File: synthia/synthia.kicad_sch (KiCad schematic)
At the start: 119 parts, among them J1 MJ-63022B, J2 SJ3-35083C-TR, J3 PJ-007, J4 SDS-50J, Q1 IRF9540N, U1 TLV272IP, U2 STM32H750ZBT6, U3 LD1117V33, U4 PVA1EEH31.2NV2, U5 PVA1EEH31.2NV2, U6 ATS08A-E

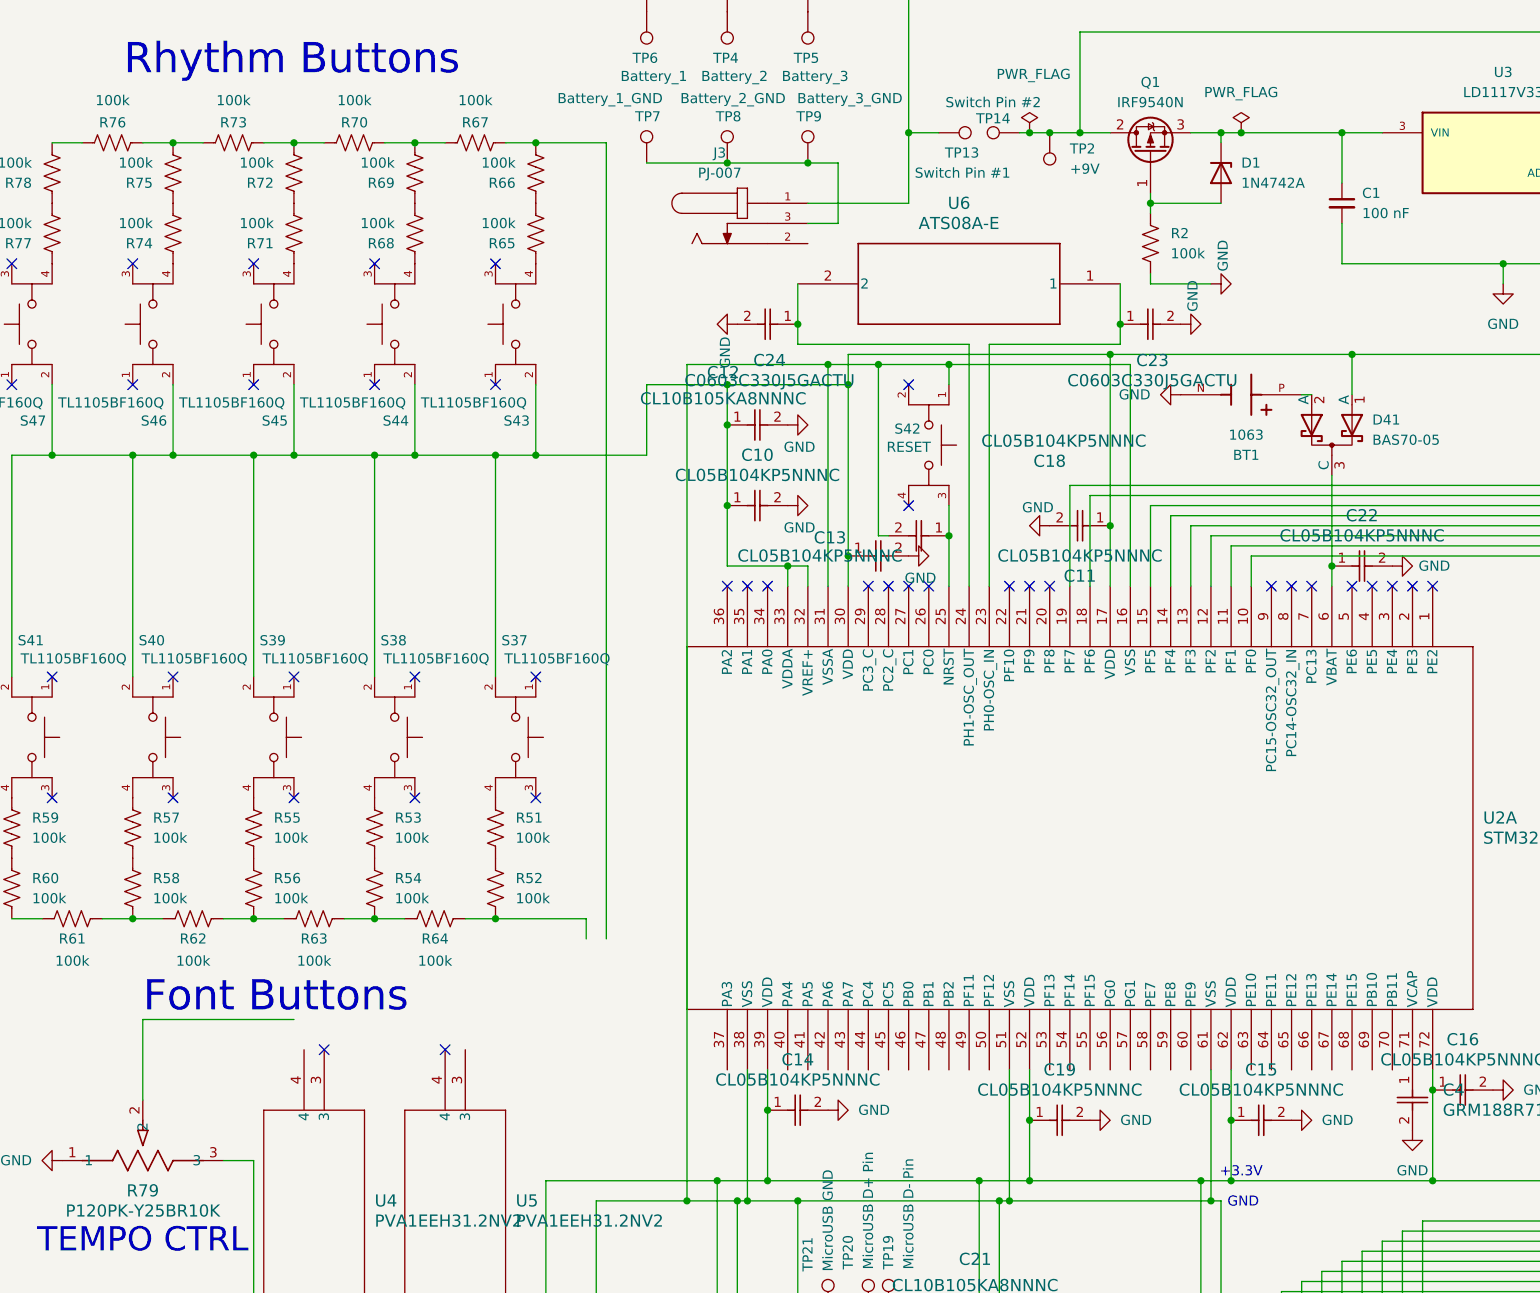
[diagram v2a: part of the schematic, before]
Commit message: made 3D model of current PCB, will likely be updated and replaced when needed
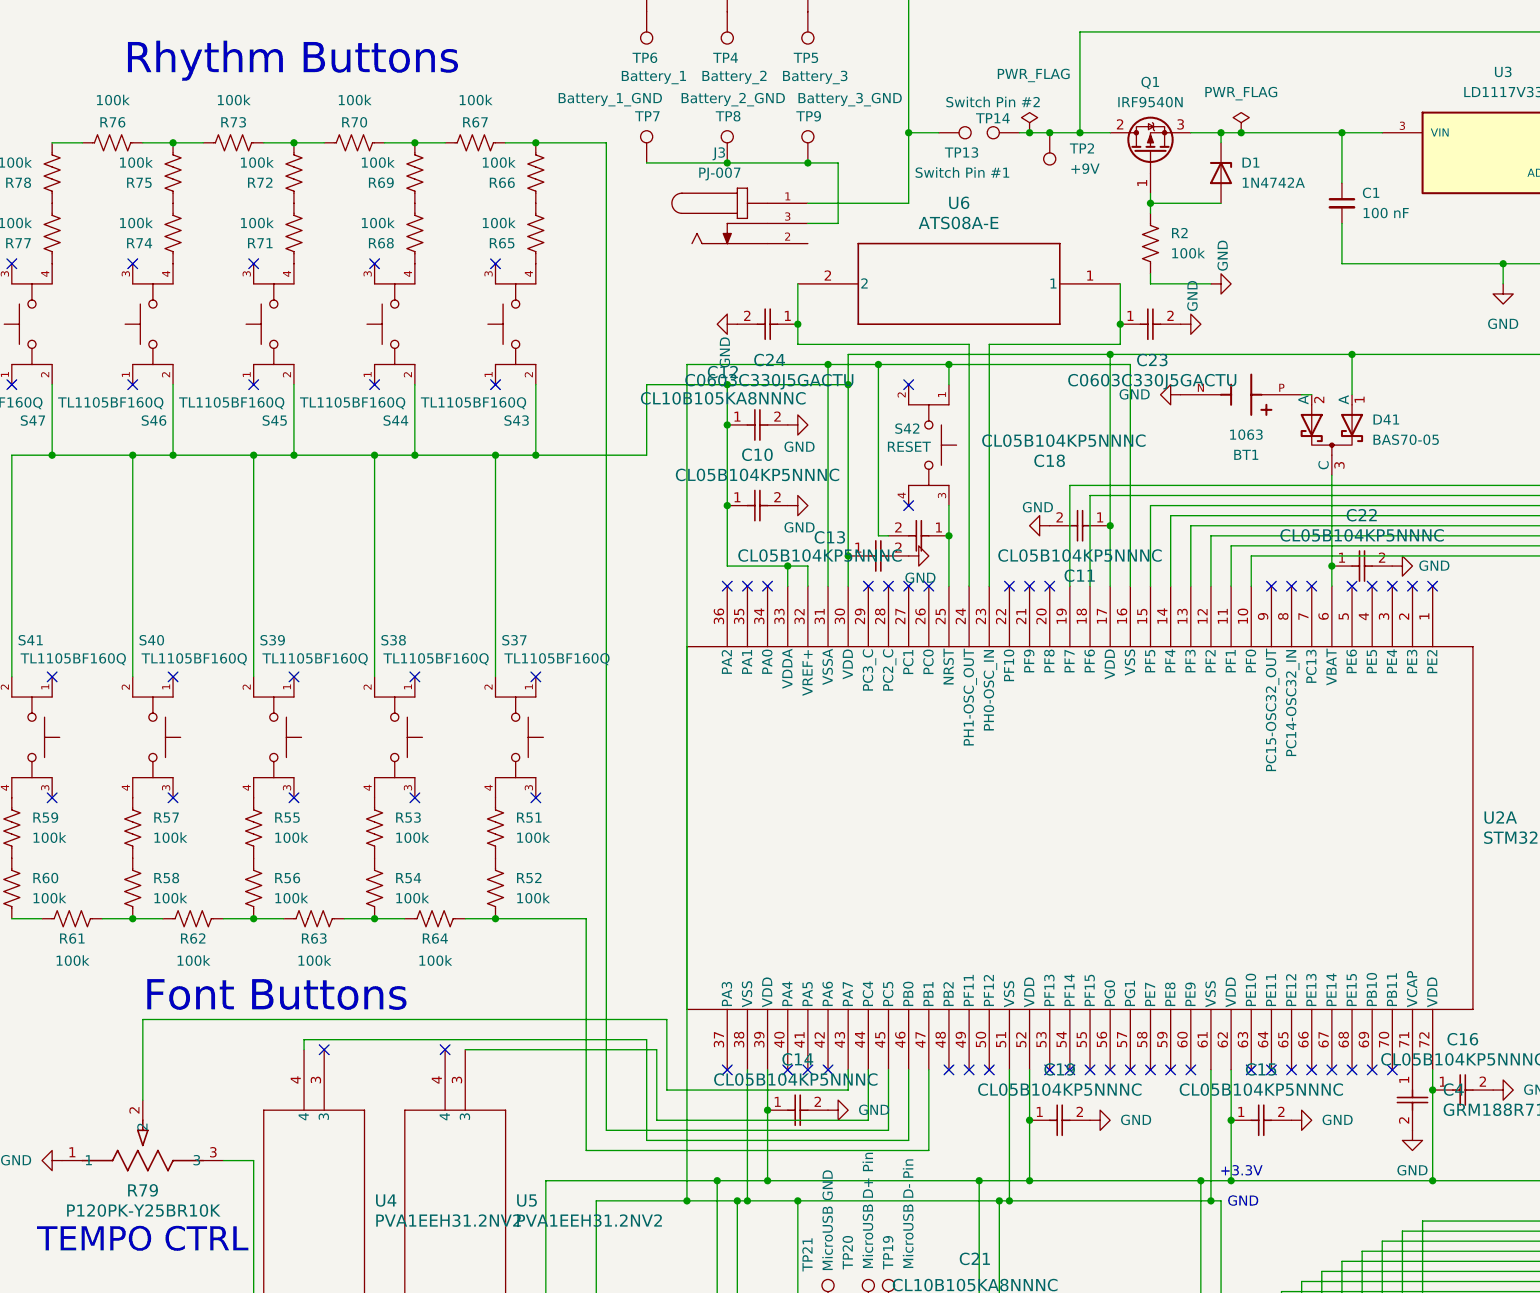
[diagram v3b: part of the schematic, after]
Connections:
- net at R66.2, R67.1: now also U2.45 (PC5)
- net at R52.2, R64.2: now also U2.47 (PB1)
- net at U4.4: now also U2.46 (PB0)
- net at R79.2: now also U2.43 (PA7)
- net at U2.44 (PC4): now also U5.3
- no-connect marks 86 -> 109
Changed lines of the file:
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@@
 	)
 	(no_connect
+		(at 134.62 161.29)
+	)
+	(no_connect
 		(at 120.65 205.74)
 	)
 	(no_connect
+		(at 154.94 161.29)
+	)
+	(no_connect
 		(at 180.34 100.33)
 	)
 	(no_connect
+		(at 139.7 161.29)
+	)
+	(no_connect
+		(at 190.5 161.29)
+	)
+	(no_connect
 		(at 168.91 256.54)
 	)
 	(no_connect
+		(at 137.16 161.29)
+	)
+	(no_connect
 		(at 82.55 127)
 	)
@@
 	)
 	(no_connect
+		(at 162.56 161.29)
+	)
+	(no_connect
 		(at 171.45 256.54)
 	)
@@
 	)
 	(no_connect
+		(at 160.02 161.29)
+	)
+	(no_connect
 		(at 146.05 205.74)
 	)
@@
 	)
 	(no_connect
+		(at 114.3 161.29)
+	)
+	(no_connect
 		(at 129.54 90.17)
 	)
 	(no_connect
+		(at 187.96 161.29)
+	)
+	(no_connect
 		(at 31.75 59.69)
 	)
@@
 	)
 	(no_connect
+		(at 165.1 161.29)
+	)
+	(no_connect
 		(at 128.27 256.54)
 	)
@@
 	)
 	(no_connect
+		(at 185.42 161.29)
+	)
+	(no_connect
 		(at 148.59 205.74)
 	)
@@
 	)
 	(no_connect
+		(at 182.88 161.29)
+	)
+	(no_connect
 		(at 166.37 256.54)
 	)
@@
 	)
 	(no_connect
+		(at 157.48 161.29)
+	)
+	(no_connect
 		(at 185.42 100.33)
 	)
@@
 	)
 	(no_connect
+		(at 147.32 161.29)
+	)
+	(no_connect
 		(at 156.21 256.54)
 	)
@@
 	)
 	(no_connect
+		(at 106.68 161.29)
+	)
+	(no_connect
 		(at 143.51 256.54)
 	)
@@
 	)
 	(no_connect
+		(at 177.8 161.29)
+	)
+	(no_connect
 		(at 181.61 256.54)
 	)
 	(no_connect
+		(at 149.86 161.29)
+	)
+	(no_connect
 		(at 151.13 256.54)
 	)
@@
 	)
 	(no_connect
+		(at 116.84 161.29)
+	)
+	(no_connect
+		(at 152.4 161.29)
+	)
+	(no_connect
 		(at 21.59 127)
 	)
@@
 	)
 	(no_connect
+		(at 119.38 161.29)
+	)
+	(no_connect
 		(at 55.88 158.75)
 	)
@@
 	)
 	(no_connect
+		(at 180.34 161.29)
+	)
+	(no_connect
 		(at 111.76 100.33)
 	)
@@
 	)
 	(no_connect
+		(at 175.26 161.29)
+	)
+	(no_connect
 		(at 71.12 199.39)
 	)
@@
 	)
 	(no_connect
+		(at 172.72 161.29)
+	)
+	(no_connect
 		(at 125.73 256.54)
 	)
 	(wire
 		(pts
+			(xy 53.34 158.75) (xy 53.34 157.48)
+		)
+		(stroke
+			(width 0)
+			(type default)
+		)
+	)
+	(wire
+		(pts
 			(xy 241.3 105.41) (xy 246.38 105.41)
 		)
@@
 	(wire
 		(pts
-			(xy 88.9 142.24) (xy 88.9 144.78)
+			(xy 88.9 142.24) (xy 88.9 171.45)
 		)
 		(stroke
@@
 	(wire
 		(pts
+			(xy 127 168.91) (xy 127 161.29)
+		)
+		(stroke
+			(width 0)
+			(type default)
+		)
+	)
+	(wire
+		(pts
 			(xy 129.54 43.18) (xy 129.54 52.07)
 		)
@@
 	(wire
 		(pts
+			(xy 97.79 158.75) (xy 97.79 167.64)
+		)
+		(stroke
+			(width 0)
+			(type default)
+		)
+	)
+	(wire
+		(pts
 			(xy 116.84 20.32) (xy 129.54 20.32)
 		)
@@
 	(wire
 		(pts
+			(xy 99.06 154.94) (xy 99.06 163.83)
+		)
+		(stroke
+			(width 0)
+			(type default)
+		)
+	)
+	(wire
+		(pts
 			(xy 21.59 74.93) (xy 21.59 83.82)
 		)
@@
 	(wire
 		(pts
+			(xy 132.08 171.45) (xy 132.08 161.29)
+		)
+		(stroke
+			(width 0)
+			(type default)
+		)
+	)
+	(wire
+		(pts
 			(xy 242.57 193.04) (xy 163.83 193.04)
 		)
@@
 	(wire
 		(pts
+			(xy 73.66 158.75) (xy 97.79 158.75)
+		)
+		(stroke
+			(width 0)
+			(type default)
+		)
+	)
+	(wire
+		(pts
 			(xy 109.22 177.8) (xy 115.57 177.8)
 		)
@@
 	(wire
 		(pts
+			(xy 91.44 168.91) (xy 127 168.91)
+		)
+		(stroke
+			(width 0)
+			(type default)
+		)
+	)
+	(wire
+		(pts
 			(xy 237.49 93.98) (xy 237.49 120.65)
 		)
@@
 	(wire
 		(pts
+			(xy 97.79 167.64) (xy 124.46 167.64)
+		)
+		(stroke
+			(width 0)
+			(type default)
+		)
+	)
+	(wire
+		(pts
 			(xy 162.56 100.33) (xy 162.56 91.44)
 		)
@@
 	(wire
 		(pts
+			(xy 96.52 157.48) (xy 96.52 170.18)
+		)
+		(stroke
+			(width 0)
+			(type default)
+		)
+	)
+	(wire
+		(pts
 			(xy 223.52 43.18) (xy 228.6 43.18)
 		)
@@
 	(wire
 		(pts
+			(xy 88.9 171.45) (xy 132.08 171.45)
+		)
+		(stroke
+			(width 0)
+			(type default)
+		)
+	)
+	(wire
+		(pts
 			(xy 124.46 191.77) (xy 124.46 193.04)
 		)
@@
 	(wire
 		(pts
+			(xy 53.34 157.48) (xy 96.52 157.48)
+		)
+		(stroke
+			(width 0)
+			(type default)
+		)
+	)
+	(wire
+		(pts
 			(xy 195.58 163.83) (xy 195.58 175.26)
 		)
@@
 	(wire
 		(pts
+			(xy 129.54 170.18) (xy 129.54 161.29)
+		)
+		(stroke
+			(width 0)
+			(type default)
+		)
+	)
+	(wire
+		(pts
 			(xy 167.64 177.8) (xy 168.91 177.8)
 		)
@@
 	(wire
 		(pts
+			(xy 96.52 170.18) (xy 129.54 170.18)
+		)
+		(stroke
+			(width 0)
+			(type default)
+		)
+	)
+	(wire
+		(pts
 			(xy 120.65 46.99) (xy 116.84 46.99)
 		)
@@
 	(wire
 		(pts
-			(xy 33.02 154.94) (xy 52.07 154.94)
+			(xy 33.02 154.94) (xy 99.06 154.94)
 		)
 		(stroke
@@
 	(wire
 		(pts
-			(xy 52.07 74.93) (xy 52.07 83.82)
+			(xy 124.46 167.64) (xy 124.46 161.29)
 		)
 		(stroke
@@
 	(wire
 		(pts
-			(xy 96.52 83.82) (xy 96.52 74.93)
+			(xy 52.07 74.93) (xy 52.07 83.82)
 		)
 		(stroke
@@
 	(wire
 		(pts
-			(xy 91.44 44.45) (xy 91.44 144.78)
+			(xy 96.52 83.82) (xy 96.52 74.93)
 		)
 		(stroke
@@
 	(wire
 		(pts
+			(xy 99.06 163.83) (xy 121.92 163.83)
+		)
+		(stroke
+			(width 0)
+			(type default)
+		)
+	)
+	(wire
+		(pts
+			(xy 91.44 44.45) (xy 91.44 168.91)
+		)
+		(stroke
+			(width 0)
+			(type default)
+		)
+	)
+	(wire
+		(pts
 			(xy 184.15 59.69) (xy 184.15 54.61)
 		)
@@
 	(wire
 		(pts
+			(xy 121.92 163.83) (xy 121.92 161.29)
+		)
+		(stroke
+			(width 0)
+			(type default)
+		)
+	)
+	(wire
+		(pts
 			(xy 115.57 191.77) (xy 115.57 177.8)
 		)
@@
 		(in_pos_files yes)
 		(dnp no)
-		(fields_autoplaced yes)
 		(property "Reference" "C14"
 			(at 115.57 160.02 0)
@@
 		)
 		(property "Value" "CL05B104KP5NNNC"
-			(at 115.57 162.56 0)
+			(at 115.316 162.56 0)
 			(show_name no)
 			(do_not_autoplace no)
